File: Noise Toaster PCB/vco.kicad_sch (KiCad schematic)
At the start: 16 parts, among them J5 VCO, Q3 2N3904, Q4 2N3904, U1 LM324

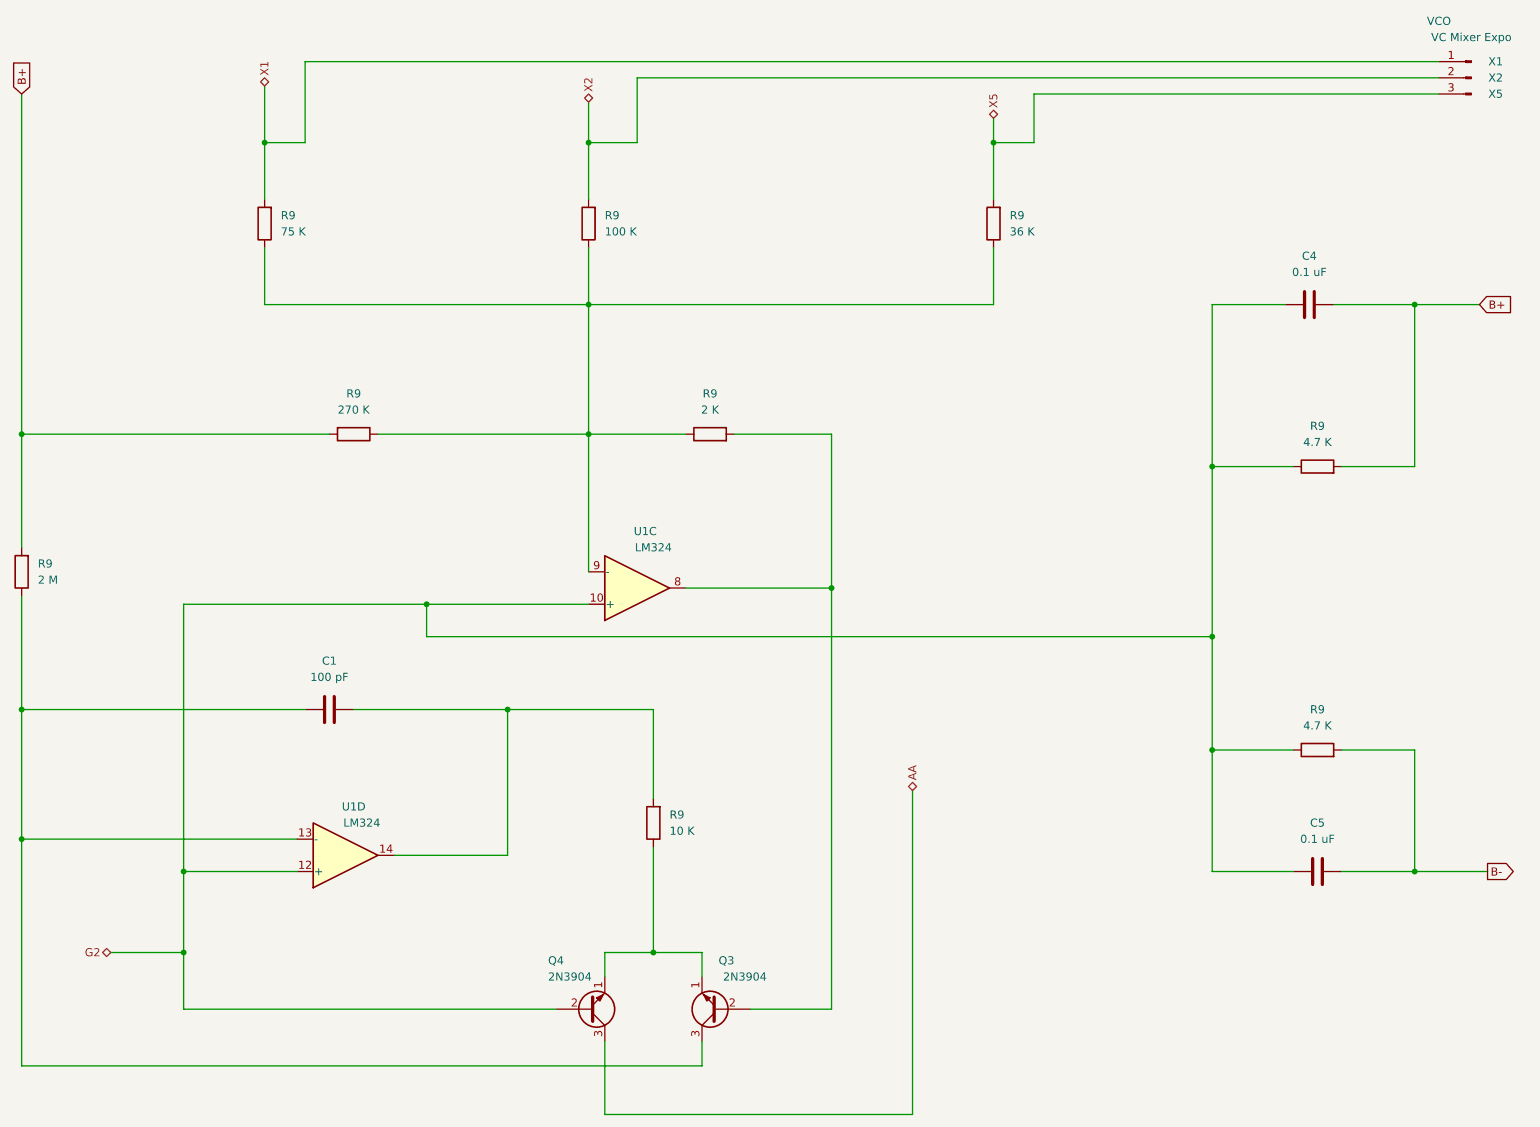
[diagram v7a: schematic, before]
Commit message: added front panel pcb
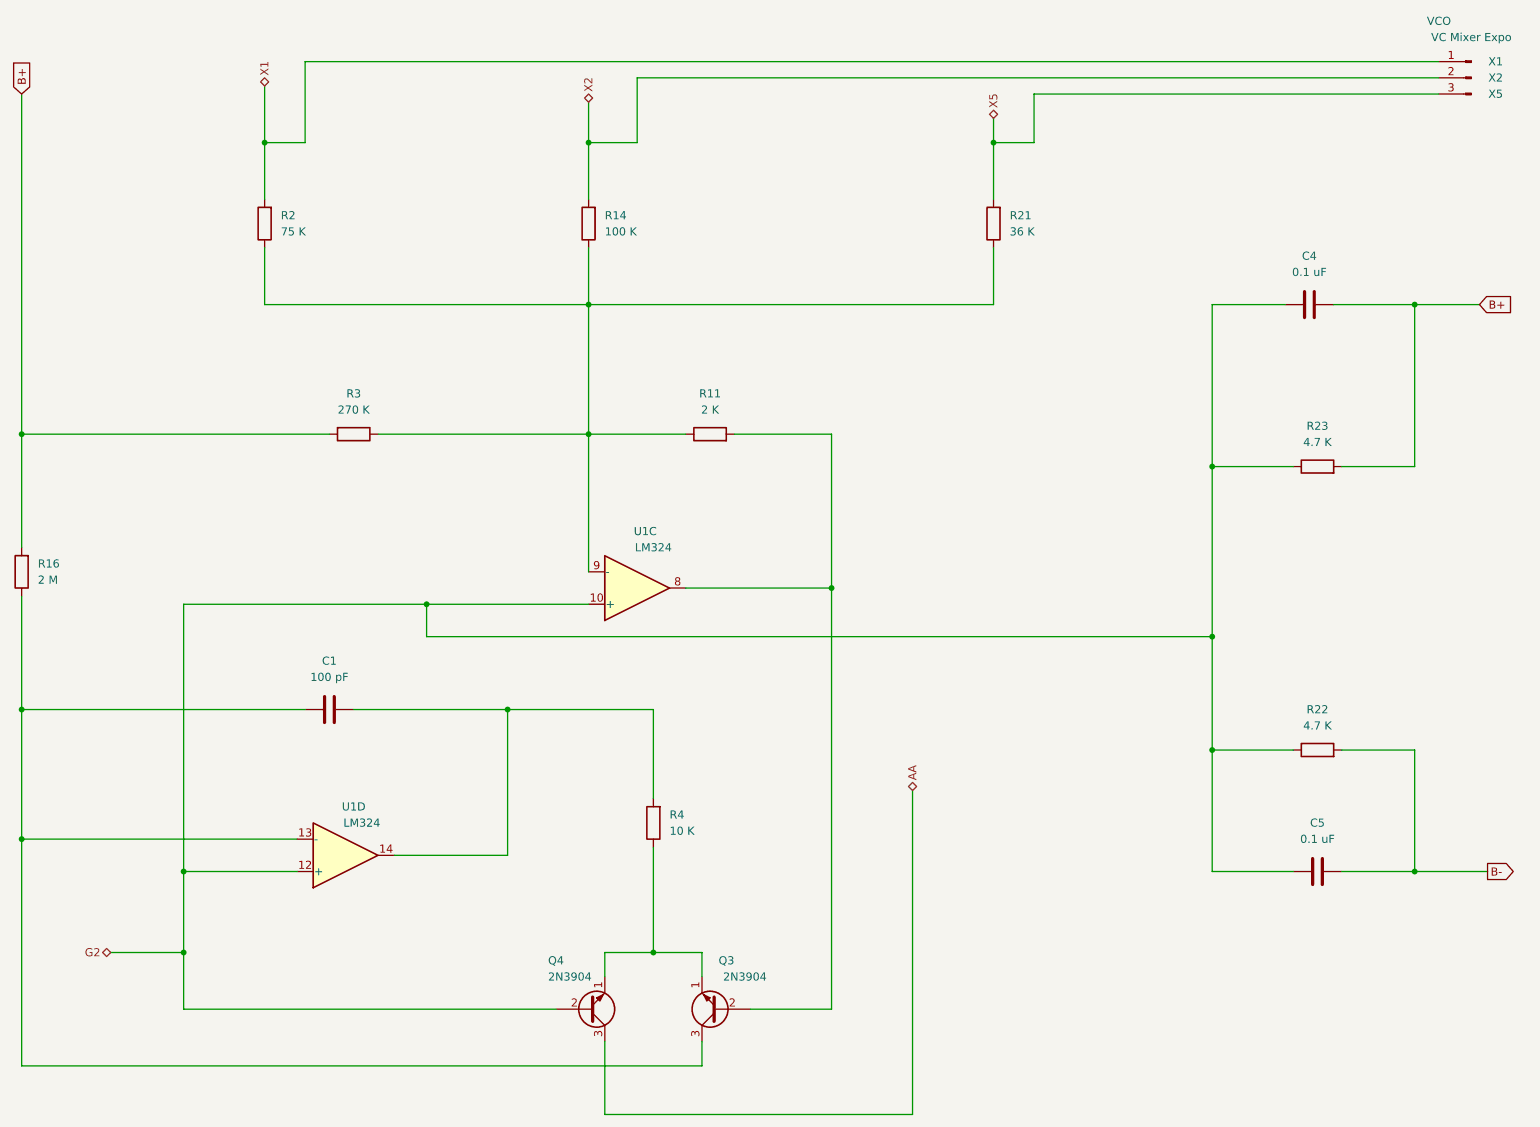
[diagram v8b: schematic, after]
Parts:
- renumbered R9 to R11, R9 to R14, R9 to R16, R9 to R2, R9 to R21, R9 to R22, R9 to R23, R9 to R3, R9 to R4
